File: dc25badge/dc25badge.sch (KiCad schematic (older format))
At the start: 33 parts, among them P1 BATT, P2 USB_OTG, P3 CORTEX, SW1 RESET, SW3 MODE, SW4 BRIGHT, U1 MIC5305, U2 TPS61232, U3 ATSAMD21E18A-AU, U4 74AHCT125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

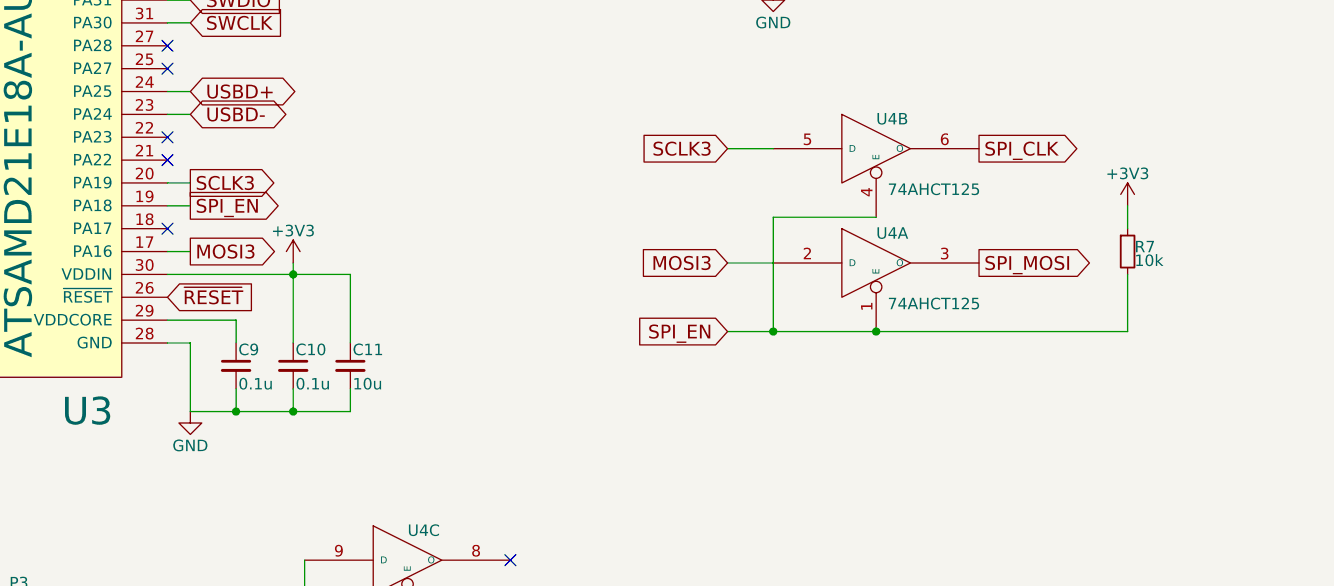
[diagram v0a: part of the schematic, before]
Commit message: Remove use of CS line.
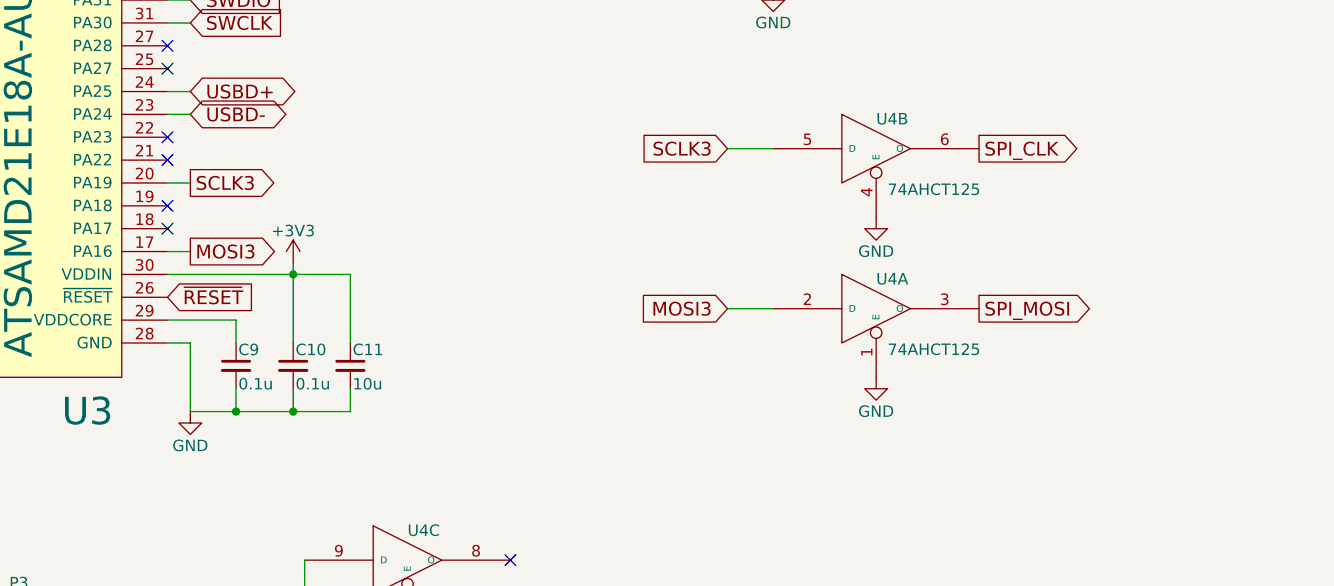
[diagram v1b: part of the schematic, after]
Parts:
- removed R7: 10k, Resistors_SMD:R_0805_HandSoldering, symbol R_Small
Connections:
- net GND: now also U4.1 (E), U4.4 (E)
- removed net SPI_EN: U3.19 (PA18), U4.1 (E), U4.4 (E)
- no-connect marks 26 -> 27
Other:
- moved on the sheet: U4A
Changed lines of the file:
@@
-$EndComp
-$Comp
-L 74AHCT125 U4
-U 1 1 592AB1CD
-P 6750 5100
-F 0 "U4" H 6750 5200 50  0000 L BNN
-F 1 "74AHCT125" H 6800 4950 50  0000 L TNN
-F 2 "SMD_Packages:SOIC-14_N" H 6750 5100 50  0001 C CNN
-F 3 "" H 6750 5100 50  0000 C CNN
-	1    6750 5100
-	1    0    0    -1
 $EndComp
 $Comp
@@
 Text GLabel 7200 4600 2    60   Output ~ 0
 SPI_CLK
-Text GLabel 7200 5100 2    60   Output ~ 0
+Text GLabel 7200 5300 2    60   Output ~ 0
 SPI_MOSI
-$Comp
-L R_Small R7
-U 1 1 592AC590
-P 7850 5050
-F 0 "R7" H 7880 5070 50  0000 L CNN
-F 1 "10k" H 7880 5010 50  0000 L CNN
-F 2 "Resistors_SMD:R_0805_HandSoldering" H 7850 5050 50  0001 C CNN
-F 3 "" H 7850 5050 50  0000 C CNN
-	1    7850 5050
-	1    0    0    -1
-$EndComp
-$Comp
-L +3V3 #PWR015
-U 1 1 592AC6CD
-P 7850 4850
-F 0 "#PWR015" H 7850 4700 50  0001 C CNN
-F 1 "+3V3" H 7850 4990 50  0000 C CNN
-F 2 "" H 7850 4850 50  0000 C CNN
-F 3 "" H 7850 4850 50  0000 C CNN
-	1    7850 4850
-	1    0    0    -1
-$EndComp
 $Comp
 L GND #PWR016
@@
 Wire Wire Line
 	1250 4250 1250 4150
-Wire Wire Line
-	6100 5400 7850 5400
-Wire Wire Line
-	7850 5400 7850 5150
-Connection ~ 6750 5400
-Wire Wire Line
-	7850 4850 7850 4950
 $Comp
 L 74AHCT125 U4
@@
 Text GLabel 3750 4750 2    60   Output ~ 0
 SCLK3
-Text GLabel 3750 4850 2    60   Output ~ 0
-SPI_EN
-Wire Wire Line
-	3750 4850 3650 4850
 Wire Wire Line
 	3750 5050 3650 5050
 Text GLabel 6100 4600 0    60   Input ~ 0
 SCLK3
-Text GLabel 6100 5100 0    60   Input ~ 0
+Text GLabel 6100 5300 0    60   Input ~ 0
 MOSI3
 Wire Wire Line
-	6300 5100 6100 5100
+	6300 5300 6100 5300
 Wire Wire Line
 	6300 4600 6100 4600
-Text GLabel 6100 5400 0    60   Input ~ 0
-SPI_EN
-Wire Wire Line
-	6750 4900 6300 4900
-Wire Wire Line
-	6300 4900 6300 5400
-Connection ~ 6300 5400
 Text GLabel 2200 4650 0    60   Input ~ 0
 BRIGHT
@@
 	6300 3550 6300 3900
 NoConn ~ 2300 4450
+NoConn ~ 3650 4850
+$Comp
+L 74AHCT125 U4
+U 1 1 592AB1CD
+P 6750 5300
+F 0 "U4" H 6750 5400 50  0000 L BNN
+F 1 "74AHCT125" H 6800 5150 50  0000 L TNN
+F 2 "SMD_Packages:SOIC-14_N" H 6750 5300 50  0001 C CNN
+F 3 "" H 6750 5300 50  0000 C CNN
+	1    6750 5300
+	1    0    0    -1
+$EndComp
+$Comp
+L GND #PWR?
+U 1 1 59345803
+P 6750 4900
+F 0 "#PWR?" H 6750 4650 50  0001 C CNN
+F 1 "GND" H 6750 4750 50  0000 C CNN
+F 2 "" H 6750 4900 50  0000 C CNN
+F 3 "" H 6750 4900 50  0000 C CNN
+	1    6750 4900
+	1    0    0    -1
+$EndComp
+$Comp
+L GND #PWR?
+U 1 1 5934585D
+P 6750 5600
+F 0 "#PWR?" H 6750 5350 50  0001 C CNN
+F 1 "GND" H 6750 5450 50  0000 C CNN
+F 2 "" H 6750 5600 50  0000 C CNN
+F 3 "" H 6750 5600 50  0000 C CNN
+	1    6750 5600
+	1    0    0    -1
+$EndComp
 $EndSCHEMATC

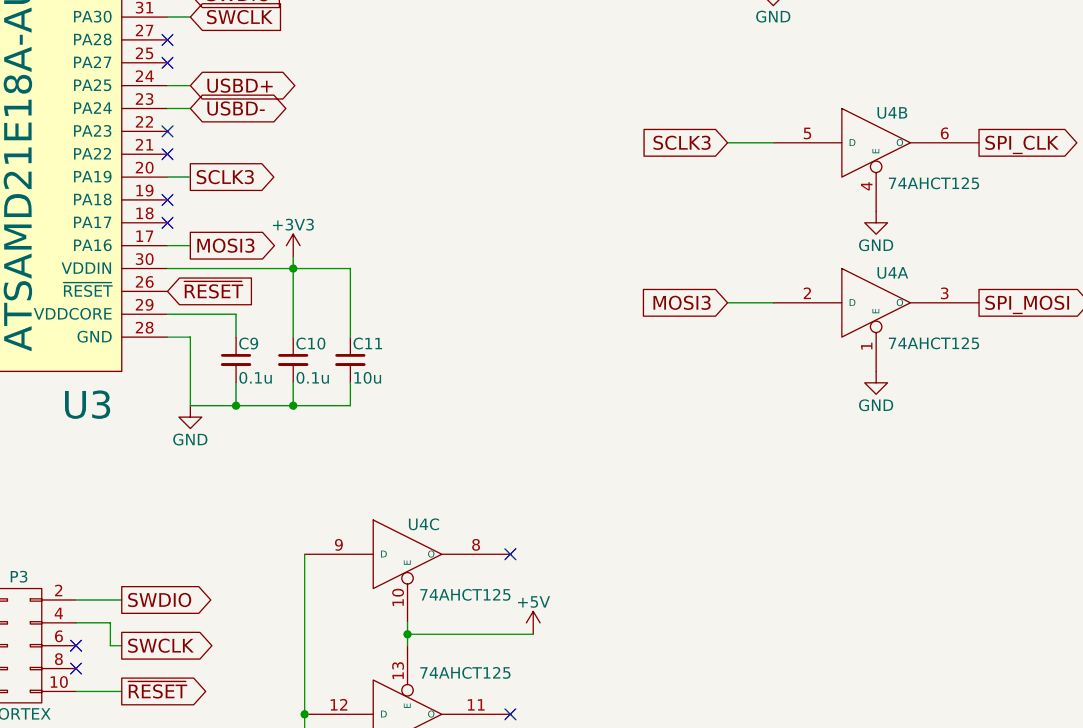
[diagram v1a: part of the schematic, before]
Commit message: Add indicator LED.
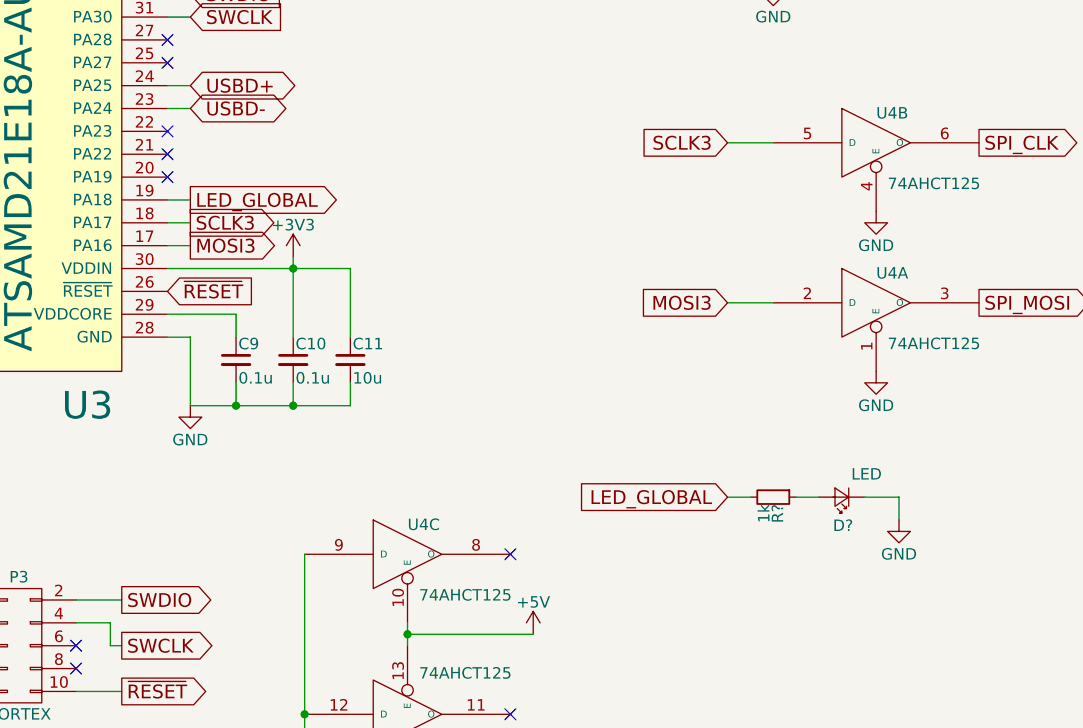
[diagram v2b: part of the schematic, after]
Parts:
- added D?: LED, symbol LED_Small
- added R?: 1k, symbol R_Small
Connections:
- net GND: now also D?.1 (K)
- net SCLK3: now also U3.18 (PA17); no longer U3.20 (PA19)
- net LED_GLOBAL: now reaches U3.19 (PA18)
- net LED_GLOBAL: now also R?.2
- new net: D?.2 (A), R?.1
- no-connect marks 27 -> 26
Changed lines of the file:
@@
 SPI_MOSI
 $Comp
-L GND #PWR016
+L GND #PWR015
 U 1 1 592ACB78
 P 5550 950
-F 0 "#PWR016" H 5550 700 50  0001 C CNN
+F 0 "#PWR015" H 5550 700 50  0001 C CNN
 F 1 "GND" H 5550 800 50  0000 C CNN
 F 2 "" H 5550 950 50  0000 C CNN
@@
 $EndComp
 $Comp
-L PWR_FLAG #FLG017
+L PWR_FLAG #FLG016
 U 1 1 592AD95C
 P 1150 1750
-F 0 "#FLG017" H 1150 1845 50  0001 C CNN
+F 0 "#FLG016" H 1150 1845 50  0001 C CNN
 F 1 "PWR_FLAG" H 1150 1930 50  0000 C CNN
 F 2 "" H 1150 1750 50  0000 C CNN
@@
 	4700 6700 4700 6800
 $Comp
-L +5V #PWR018
+L +5V #PWR017
 U 1 1 592AE3BE
 P 5250 6750
-F 0 "#PWR018" H 5250 6600 50  0001 C CNN
+F 0 "#PWR017" H 5250 6600 50  0001 C CNN
 F 1 "+5V" H 5250 6890 50  0000 C CNN
 F 2 "" H 5250 6750 50  0000 C CNN
@@
 	4250 6400 4250 7200
 $Comp
-L GND #PWR019
+L GND #PWR018
 U 1 1 592AE5B3
 P 4250 7200
-F 0 "#PWR019" H 4250 6950 50  0001 C CNN
+F 0 "#PWR018" H 4250 6950 50  0001 C CNN
 F 1 "GND" H 4250 7050 50  0000 C CNN
 F 2 "" H 4250 7200 50  0000 C CNN
@@
 NoConn ~ 3650 4550
 $Comp
-L GND #PWR020
+L GND #PWR019
 U 1 1 592B0060
 P 1350 3500
-F 0 "#PWR020" H 1350 3250 50  0001 C CNN
+F 0 "#PWR019" H 1350 3250 50  0001 C CNN
 F 1 "GND" H 1350 3350 50  0000 C CNN
 F 2 "" H 1350 3500 50  0000 C CNN
@@
 Connection ~ 2150 3250
 $Comp
-L GND #PWR021
+L GND #PWR020
 U 1 1 592B1083
 P 2350 3600
-F 0 "#PWR021" H 2350 3350 50  0001 C CNN
+F 0 "#PWR020" H 2350 3350 50  0001 C CNN
 F 1 "GND" H 2350 3450 50  0000 C CNN
 F 2 "" H 2350 3600 50  0000 C CNN
@@
 	5700 3550 5800 3550
 $Comp
-L GND #PWR022
+L GND #PWR021
 U 1 1 592BA362
 P 6300 3900
-F 0 "#PWR022" H 6300 3650 50  0001 C CNN
+F 0 "#PWR021" H 6300 3650 50  0001 C CNN
 F 1 "GND" H 6300 3750 50  0000 C CNN
 F 2 "" H 6300 3900 50  0000 C CNN
@@
 Text GLabel 3750 5050 2    60   Output ~ 0
 MOSI3
-Text GLabel 3750 4750 2    60   Output ~ 0
+Text GLabel 3750 4950 2    60   Output ~ 0
 SCLK3
 Wire Wire Line
@@
 $EndComp
 $Comp
-L GND #PWR023
+L GND #PWR022
 U 1 1 592C536E
 P 4150 2600
-F 0 "#PWR023" H 4150 2350 50  0001 C CNN
+F 0 "#PWR022" H 4150 2350 50  0001 C CNN
 F 1 "GND" H 4150 2450 50  0000 C CNN
 F 2 "" H 4150 2600 50  0000 C CNN
@@
 NoConn ~ 3700 1950
 $Comp
-L +5V #PWR024
+L +5V #PWR023
 U 1 1 592C61C0
 P 3500 2050
-F 0 "#PWR024" H 3500 1900 50  0001 C CNN
+F 0 "#PWR023" H 3500 1900 50  0001 C CNN
 F 1 "+5V" H 3500 2190 50  0000 C CNN
 F 2 "" H 3500 2050 50  0000 C CNN
@@
 NoConn ~ 1050 3300
 $Comp
-L GND #PWR025
+L GND #PWR024
 U 1 1 592CB85E
 P 850 4400
-F 0 "#PWR025" H 850 4150 50  0001 C CNN
+F 0 "#PWR024" H 850 4150 50  0001 C CNN
 F 1 "GND" H 850 4250 50  0000 C CNN
 F 2 "" H 850 4400 50  0000 C CNN
@@
 NoConn ~ 3650 4250
 Wire Wire Line
-	3750 4750 3650 4750
-NoConn ~ 3650 4950
+	3750 4950 3650 4950
 Wire Wire Line
 	3600 1850 3700 1850
@@
 	6300 3550 6300 3900
 NoConn ~ 2300 4450
-NoConn ~ 3650 4850
 $Comp
 L 74AHCT125 U4
@@
 $EndComp
 $Comp
-L GND #PWR?
+L GND #PWR025
 U 1 1 59345803
 P 6750 4900
-F 0 "#PWR?" H 6750 4650 50  0001 C CNN
+F 0 "#PWR025" H 6750 4650 50  0001 C CNN
 F 1 "GND" H 6750 4750 50  0000 C CNN
 F 2 "" H 6750 4900 50  0000 C CNN
@@
 $EndComp
 $Comp
-L GND #PWR?
+L GND #PWR026
 U 1 1 5934585D
 P 6750 5600
-F 0 "#PWR?" H 6750 5350 50  0001 C CNN
+F 0 "#PWR026" H 6750 5350 50  0001 C CNN
 F 1 "GND" H 6750 5450 50  0000 C CNN
 F 2 "" H 6750 5600 50  0000 C CNN
@@
 	1    0    0    -1
 $EndComp
+NoConn ~ 3650 4750
+Text GLabel 3750 4850 2    60   Output ~ 0
+LED_GLOBAL
+Wire Wire Line
+	3750 4850 3650 4850
+Text GLabel 6100 6150 0    60   Input ~ 0
+LED_GLOBAL
+$Comp
+L R_Small R?
+U 1 1 5934799E
+P 6300 6150
+F 0 "R?" H 6330 6170 50  0000 L CNN
+F 1 "1k" H 6330 6110 50  0000 L CNN
+F 2 "" H 6300 6150 50  0000 C CNN
+F 3 "" H 6300 6150 50  0000 C CNN
+	1    6300 6150
+	0    1    1    0
+$EndComp
+$Comp
+L LED_Small D?
+U 1 1 59347A4B
+P 6600 6150
+F 0 "D?" H 6550 6275 50  0000 L CNN
+F 1 "LED" H 6425 6050 50  0000 L CNN
+F 2 "" V 6600 6150 50  0000 C CNN
+F 3 "" V 6600 6150 50  0000 C CNN
+	1    6600 6150
+	-1   0    0    1
+$EndComp
+$Comp
+L GND #PWR?
+U 1 1 59347BAA
+P 6850 6250
+F 0 "#PWR?" H 6850 6000 50  0001 C CNN
+F 1 "GND" H 6850 6100 50  0000 C CNN
+F 2 "" H 6850 6250 50  0000 C CNN
+F 3 "" H 6850 6250 50  0000 C CNN
+	1    6850 6250
+	1    0    0    -1
+$EndComp
+Wire Wire Line
+	6100 6150 6200 6150
+Wire Wire Line
+	6400 6150 6500 6150
+Wire Wire Line
+	6700 6150 6850 6150
+Wire Wire Line
+	6850 6150 6850 6250
 $EndSCHEMATC

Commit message: Footprint fixes.
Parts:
- D1: renamed from D?; footprint (none) -> LEDs:LED_0805
- R1: renamed from R?; value 1k -> 330; footprint (none) -> Resistors_SMD:R_0805_HandSoldering
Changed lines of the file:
@@
 LED_GLOBAL
 $Comp
-L R_Small R?
+L R_Small R1
 U 1 1 5934799E
 P 6300 6150
-F 0 "R?" H 6330 6170 50  0000 L CNN
-F 1 "1k" H 6330 6110 50  0000 L CNN
-F 2 "" H 6300 6150 50  0000 C CNN
+F 0 "R1" H 6330 6170 50  0000 L CNN
+F 1 "330" H 6330 6110 50  0000 L CNN
+F 2 "Resistors_SMD:R_0805_HandSoldering" H 6300 6150 50  0001 C CNN
 F 3 "" H 6300 6150 50  0000 C CNN
 	1    6300 6150
@@
 $EndComp
 $Comp
-L LED_Small D?
+L LED_Small D1
 U 1 1 59347A4B
 P 6600 6150
-F 0 "D?" H 6550 6275 50  0000 L CNN
+F 0 "D1" H 6550 6275 50  0000 L CNN
 F 1 "LED" H 6425 6050 50  0000 L CNN
-F 2 "" V 6600 6150 50  0000 C CNN
+F 2 "LEDs:LED_0805" V 6600 6150 50  0001 C CNN
 F 3 "" V 6600 6150 50  0000 C CNN
 	1    6600 6150
@@
 $EndComp
 $Comp
-L GND #PWR?
+L GND #PWR027
 U 1 1 59347BAA
 P 6850 6250
-F 0 "#PWR?" H 6850 6000 50  0001 C CNN
+F 0 "#PWR027" H 6850 6000 50  0001 C CNN
 F 1 "GND" H 6850 6100 50  0000 C CNN
 F 2 "" H 6850 6250 50  0000 C CNN
